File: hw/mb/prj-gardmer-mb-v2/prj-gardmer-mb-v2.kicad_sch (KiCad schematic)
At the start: 4 parts, among them J2 230VAC_IN, J3 Conn_01x04, J4 5VDC_IN

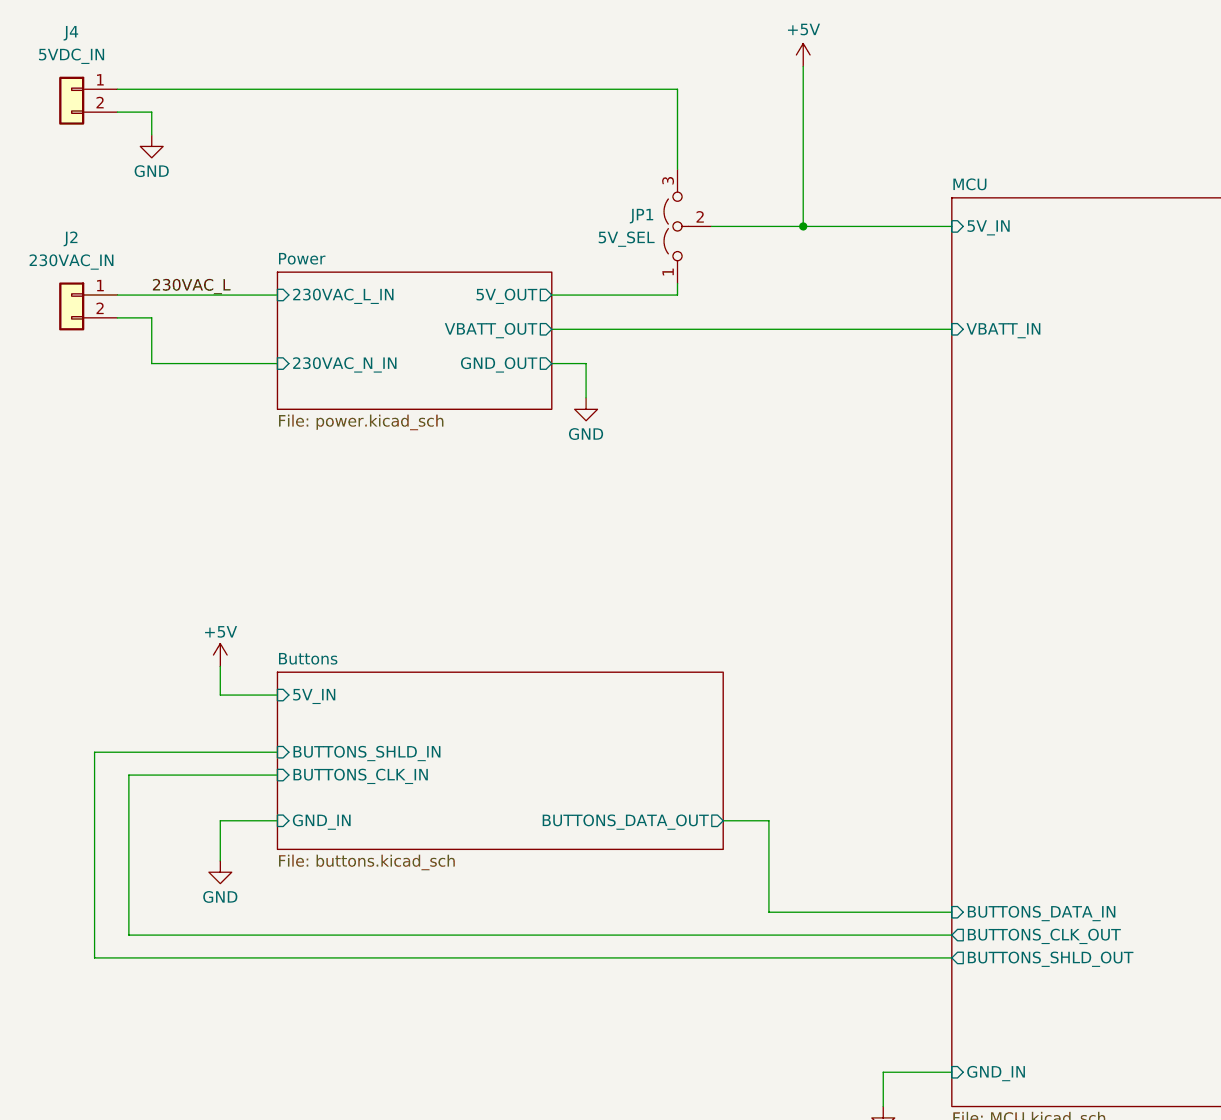
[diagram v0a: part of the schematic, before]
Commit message: Added footprints and bom. Updated schematics.
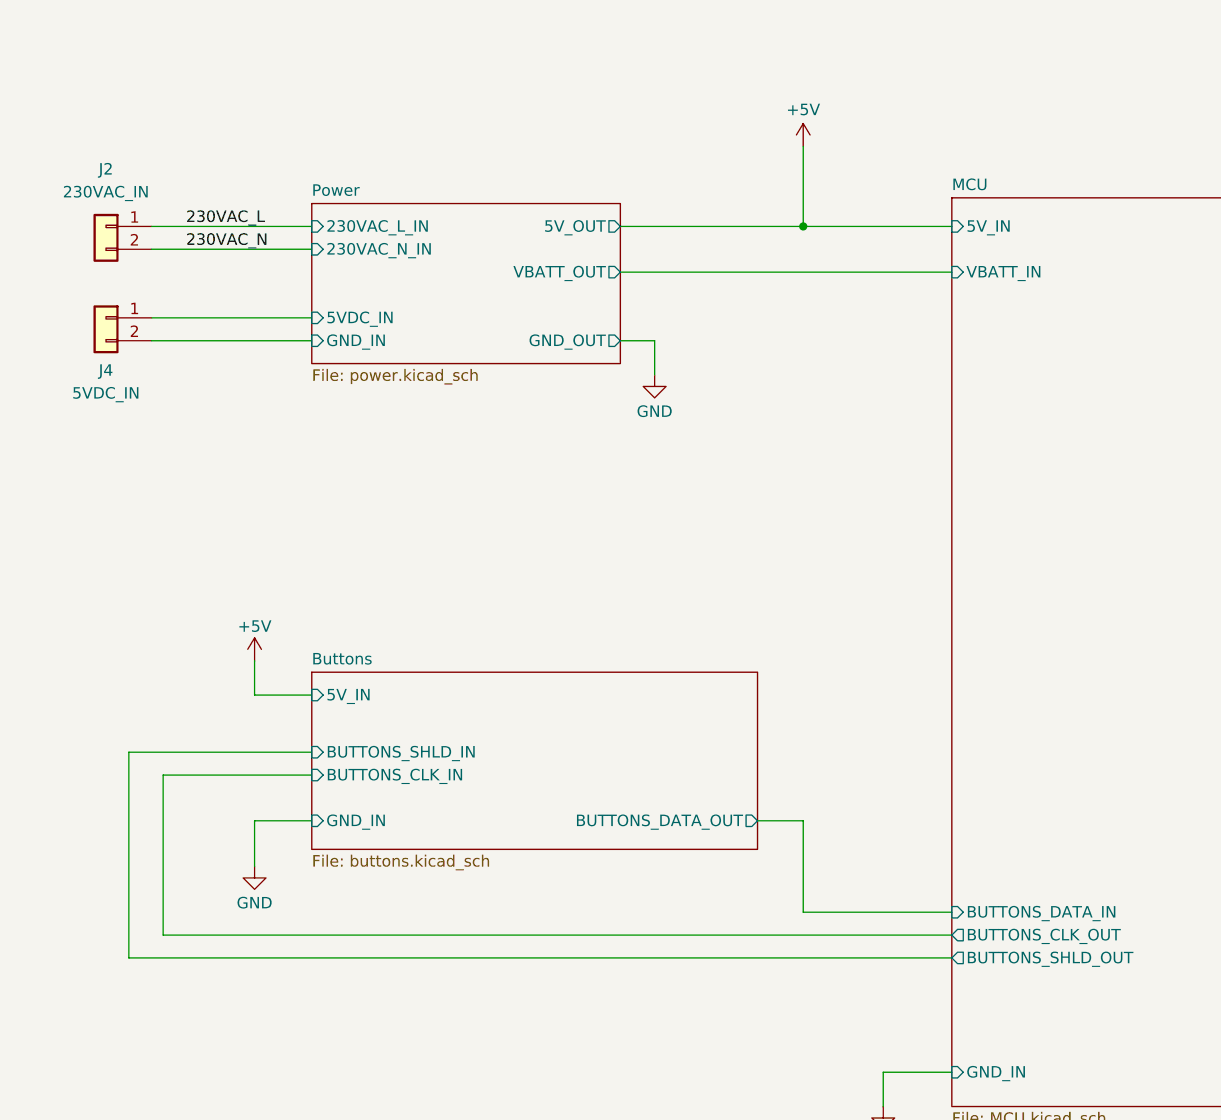
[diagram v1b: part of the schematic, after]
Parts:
- removed JP1: 5V_SEL, symbol alf64:Jumper_3_Open
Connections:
- net GND: no longer J4.2 (Pin_2)
- net Power/5VDC_IN: now reaches J4.1 (Pin_1)
- net Power/230VAC_N_IN renamed 230VAC_N
- new net Power/GND_IN: J4.2 (Pin_2)
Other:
- sheet Power ports: added 5VDC_IN, GND_IN; removed none
- moved on the sheet: J2, J4

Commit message: Assigned footprints to schematic symbols.
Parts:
- J2: footprint (none) -> alf64:PhoenixContact_MSTBA_2,5_2-G-5,08_1x02_P5.08mm_Horizontal
- J3: footprint (none) -> alf64:PhoenixContact_MSTBA_2,5_4-G-5,08_1x04_P5.08mm_Horizontal
- J4: footprint (none) -> alf64:Conn_Degson_2x3.81mm
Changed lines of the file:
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@@
 			)
 		)
-		(property "Footprint" ""
+		(property "Footprint" "alf64:PhoenixContact_MSTBA_2,5_2-G-5,08_1x02_P5.08mm_Horizontal"
 			(at 25.4 41.91 0)
 			(effects
@@
 			)
 		)
-		(property "Footprint" ""
+		(property "Footprint" "alf64:PhoenixContact_MSTBA_2,5_4-G-5,08_1x04_P5.08mm_Horizontal"
 			(at 267.97 34.29 0)
 			(effects
@@
 			)
 		)
-		(property "Footprint" ""
+		(property "Footprint" "alf64:Conn_Degson_2x3.81mm"
 			(at 25.4 52.07 0)
 			(effects

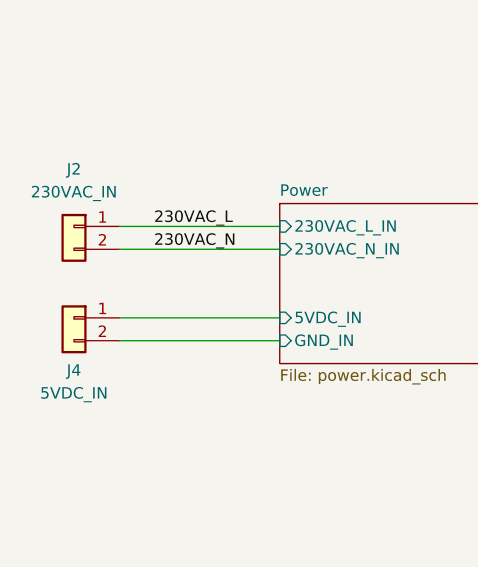
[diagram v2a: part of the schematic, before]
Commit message: Updated schematic: - added test points instead of connections between relays and outputs - fixed crystal connection for rtc
Updated PCB:
- halfway through the routing

Updated footprints:
- added footprints for test points
- reduced size of pads for D_SMA
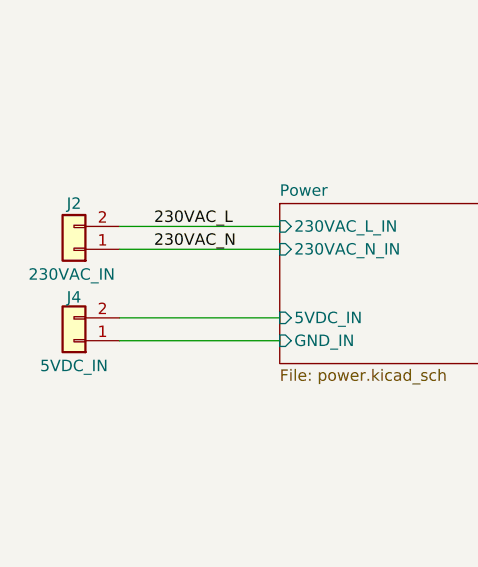
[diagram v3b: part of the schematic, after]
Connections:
- net 230VAC_L: now also J2.2 (Pin_2); no longer J2.1 (Pin_1)
- net 230VAC_N: now also J2.1 (Pin_1); no longer J2.2 (Pin_2)
- net Power/5VDC_IN: now also J4.2 (Pin_2); no longer J4.1 (Pin_1)
- net Power/GND_IN: now also J4.1 (Pin_1); no longer J4.2 (Pin_2)
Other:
- moved on the sheet: J2, J4
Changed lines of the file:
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@@
+	(wire
+		(pts
+			(xy 30.48 54.61) (xy 48.26 54.61)
+		)
+		(stroke
+			(width 0)
+			(type default)
+		)
+	)
 	(wire
 		(pts
@@
 	(wire
 		(pts
-			(xy 30.48 54.61) (xy 48.26 54.61)
-		)
-		(stroke
-			(width 0)
-			(type default)
-		)
-	)
-	(wire
-		(pts
 			(xy 86.36 58.42) (xy 86.36 54.61)
 		)
@@
 	(wire
 		(pts
+			(xy 31.75 120.65) (xy 119.38 120.65)
+		)
+		(stroke
+			(width 0)
+			(type default)
+		)
+	)
+	(wire
+		(pts
+			(xy 27.94 123.19) (xy 119.38 123.19)
+		)
+		(stroke
+			(width 0)
+			(type default)
+		)
+	)
+	(wire
+		(pts
+			(xy 203.2 128.27) (xy 198.12 128.27)
+		)
+		(stroke
+			(width 0)
+			(type default)
+		)
+	)
+	(wire
+		(pts
+			(xy 102.87 118.11) (xy 119.38 118.11)
+		)
+		(stroke
+			(width 0)
+			(type default)
+		)
+	)
+	(wire
+		(pts
+			(xy 246.38 36.83) (xy 262.89 36.83)
+		)
+		(stroke
+			(width 0)
+			(type default)
+		)
+	)
+	(wire
+		(pts
+			(xy 82.55 41.91) (xy 102.87 41.91)
+		)
+		(stroke
+			(width 0)
+			(type default)
+		)
+	)
+	(wire
+		(pts
+			(xy 173.99 123.19) (xy 203.2 123.19)
+		)
+		(stroke
+			(width 0)
+			(type default)
+		)
+	)
+	(wire
+		(pts
+			(xy 184.15 104.14) (xy 184.15 53.34)
+		)
+		(stroke
+			(width 0)
+			(type default)
+		)
+	)
+	(wire
+		(pts
 			(xy 30.48 52.07) (xy 48.26 52.07)
-		)
-		(stroke
-			(width 0)
-			(type default)
-		)
-	)
-	(wire
-		(pts
-			(xy 31.75 120.65) (xy 119.38 120.65)
-		)
-		(stroke
-			(width 0)
-			(type default)
-		)
-	)
-	(wire
-		(pts
-			(xy 27.94 123.19) (xy 119.38 123.19)
-		)
-		(stroke
-			(width 0)
-			(type default)
-		)
-	)
-	(wire
-		(pts
-			(xy 203.2 128.27) (xy 198.12 128.27)
-		)
-		(stroke
-			(width 0)
-			(type default)
-		)
-	)
-	(wire
-		(pts
-			(xy 102.87 118.11) (xy 119.38 118.11)
-		)
-		(stroke
-			(width 0)
-			(type default)
-		)
-	)
-	(wire
-		(pts
-			(xy 246.38 36.83) (xy 262.89 36.83)
-		)
-		(stroke
-			(width 0)
-			(type default)
-		)
-	)
-	(wire
-		(pts
-			(xy 82.55 41.91) (xy 102.87 41.91)
-		)
-		(stroke
-			(width 0)
-			(type default)
-		)
-	)
-	(wire
-		(pts
-			(xy 173.99 123.19) (xy 203.2 123.19)
-		)
-		(stroke
-			(width 0)
-			(type default)
-		)
-	)
-	(wire
-		(pts
-			(xy 184.15 104.14) (xy 184.15 53.34)
 		)
 		(stroke
@@
 	(symbol
 		(lib_id "alf64:Conn_01x02")
-		(at 25.4 41.91 0)
-		(mirror y)
+		(at 25.4 44.45 180)
 		(unit 1)
 		(exclude_from_sim no)
@@
 		(on_board yes)
 		(dnp no)
-		(fields_autoplaced yes)
 		(property "Reference" "J2"
-			(at 25.4 35.56 0)
+			(at 25.4 39.37 0)
 			(effects
 				(font
@@
 		)
 		(property "Value" "230VAC_IN"
-			(at 25.4 38.1 0)
+			(at 25.146 47.244 0)
 			(effects
 				(font
@@
 		)
 		(property "Footprint" "alf64:PhoenixContact_MSTBA_2,5_2-G-5,08_1x02_P5.08mm_Horizontal"
-			(at 25.4 41.91 0)
+			(at 25.4 44.45 0)
 			(effects
 				(font
@@
 		)
 		(property "Datasheet" "~"
-			(at 25.4 41.91 0)
+			(at 25.4 44.45 0)
 			(effects
 				(font
@@
 		)
 		(property "Description" "Generic connector, single row, 01x02, script generated (kicad-library-utils/schlib/autogen/connector/)"
-			(at 25.4 41.91 0)
+			(at 25.4 44.45 0)
 			(effects
 				(font
@@
 	(symbol
 		(lib_id "alf64:Conn_01x02")
-		(at 25.4 52.07 0)
-		(mirror y)
+		(at 25.4 54.61 180)
 		(unit 1)
 		(exclude_from_sim no)
@@
 		(dnp no)
 		(property "Reference" "J4"
-			(at 25.4 57.912 0)
+			(at 25.4 49.784 0)
 			(effects
 				(font
@@
 		)
 		(property "Value" "5VDC_IN"
-			(at 25.4 60.452 0)
+			(at 25.4 57.404 0)
 			(effects
 				(font
@@
 		)
 		(property "Footprint" "alf64:Conn_Degson_2x3.81mm"
-			(at 25.4 52.07 0)
+			(at 25.4 54.61 0)
 			(effects
 				(font
@@
 		)
 		(property "Datasheet" "~"
-			(at 25.4 52.07 0)
+			(at 25.4 54.61 0)
 			(effects
 				(font
@@
 		)
 		(property "Description" "Generic connector, single row, 01x02, script generated (kicad-library-utils/schlib/autogen/connector/)"
-			(at 25.4 52.07 0)
-			(effects
-				(font
+			(at 25.4 54.61 0)
+			(effects
+				(font

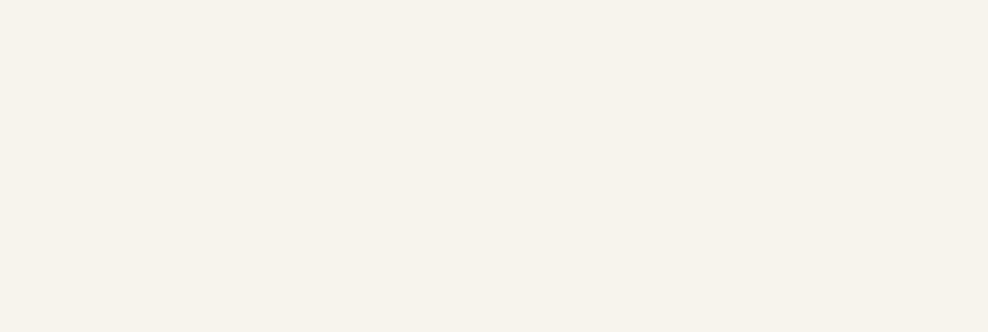
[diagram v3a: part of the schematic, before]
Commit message: Updated the hw release of prj-gardmer-mb-v2 rev001: - reorganized files in catalogues - added schematic in .pdf - added top & bottom elements on pcb in .pdf - added bom
Updated schematic:
- added a title, rev and date to the drawing info table on each sheet
- excluded test points ('TP' elements) from BOM

Updated PCB:
- added a title, rev and date to the drawing info table
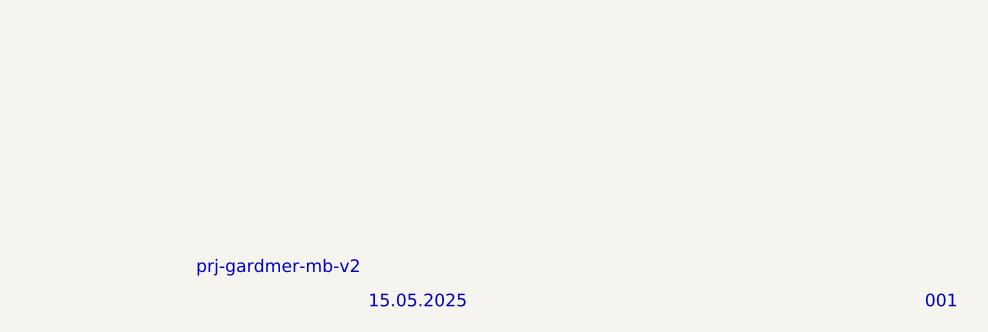
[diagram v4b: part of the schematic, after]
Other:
- note added: "001"
- note added: "15.05.2025"
- note added: "prj-gardmer-mb-v2"
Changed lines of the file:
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@@
+		)
+	)
+	(text "001"
+		(exclude_from_sim no)
+		(at 272.542 193.294 0)
+		(effects
+			(font
+				(size 1.397 1.397)
+			)
+		)
+	)
+	(text "15.05.2025"
+		(exclude_from_sim no)
+		(at 214.376 193.294 0)
+		(effects
+			(font
+				(size 1.397 1.397)
+			)
+		)
+	)
+	(text "prj-gardmer-mb-v2"
+		(exclude_from_sim no)
+		(at 198.882 189.484 0)
+		(effects
+			(font
+				(size 1.397 1.397)
+			)
 		)
 	)
